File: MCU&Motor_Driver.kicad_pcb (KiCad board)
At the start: 4 copper layers, 50 x 32.5 mm, 19 parts, among them J1 Conn_01x07_Pin, J2 Conn_01x02_Socket, J3 Conn_01x04_Pin, J4 Conn_01x03_Pin, U1 ADAFRUIT_QT_PY, U3 TMC2208-LA

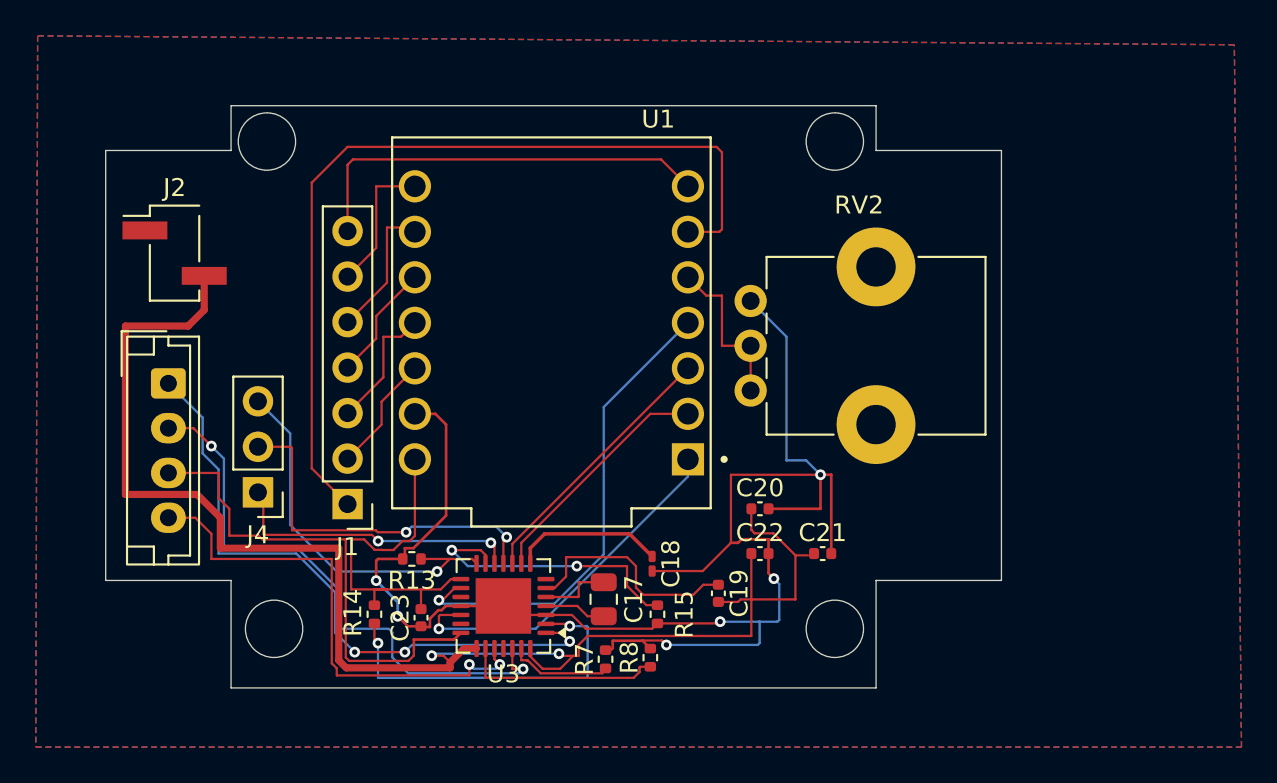
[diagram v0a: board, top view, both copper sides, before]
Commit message: Added a voltage divider to the vref pin on the TMC2208 such as to limit the max current to 0.5A based of the NEMA 14 motor I am using this for and also grounded the EN pin on the TMC2208 as to not have the need to add a GPIO connection to the ESP32 to have also that controlled since that would put too much constraints on the design and would be troublesome.
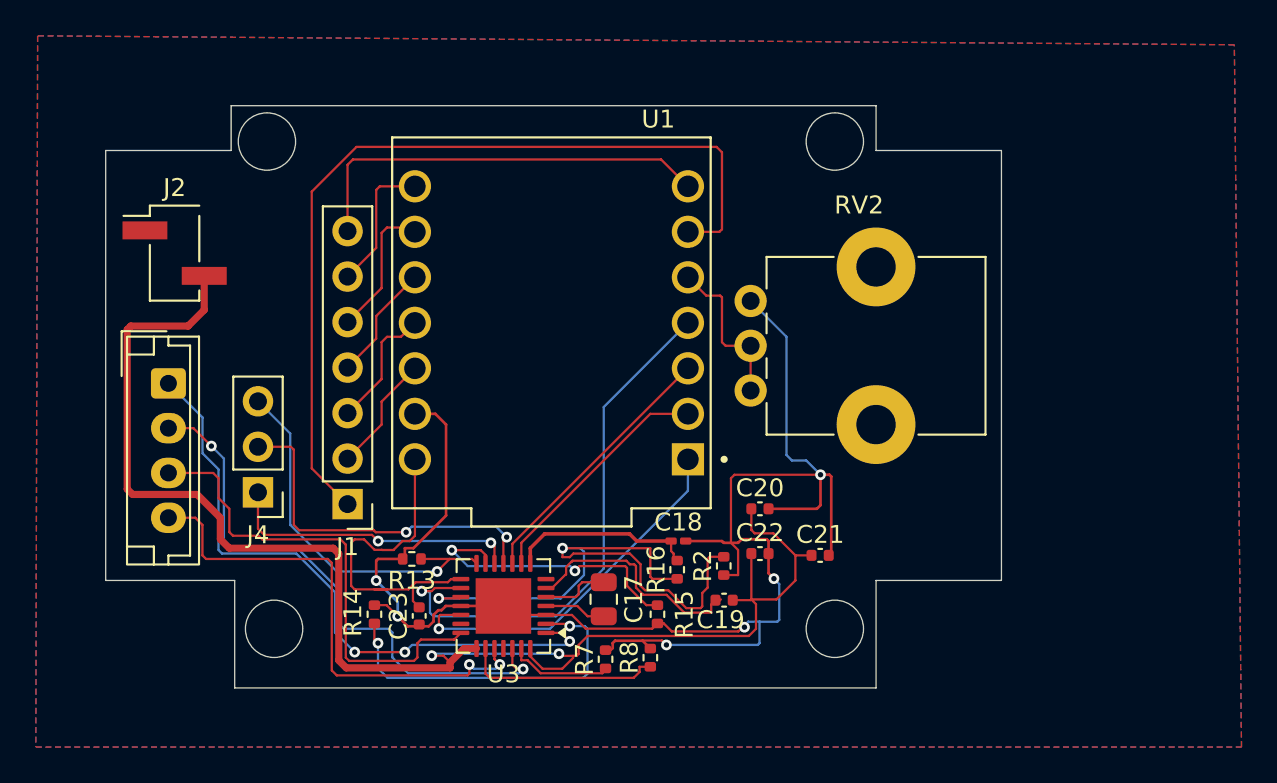
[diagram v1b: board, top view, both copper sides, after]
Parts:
- added R16: 20K, Resistor_SMD:R_0402_1005Metric, F.Cu at (158.9, 111.4)
- added R2: 3.6K, Resistor_SMD:R_0402_1005Metric, F.Cu at (161.5, 111.2)
- moved C18 1.94 mm to (159.0, 109.8), turned to 0 degrees
- moved C19 0.50 mm to (161.5, 113.1), turned to 0 degrees
- moved C21 0.17 mm to (166.9, 110.6)
- moved C23 0.14 mm to (144.5, 114.0)
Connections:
- R14 pad 1: VIO -> GND
- U3 pad 17: unconnected-(U3-VREF-Pad17) -> Net-(U3-VREF)
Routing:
- net Net-(U3-VREF): track 0.00 -> 34.7 mm, vias 0 -> 2
- net STEP: track 26.9 -> 30.4 mm
- net VM: track 84.7 -> 82.4 mm
- net +5V: track 8.50 -> 10.4 mm
- net GND: track 92.5 -> 94.1 mm
- net VIO: track 20.2 -> 19.6 mm
- net OA2: track 27.4 -> 26.9 mm
- net EN: track 20.1 -> 19.5 mm
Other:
- outline, holes or cut-outs redrawn
